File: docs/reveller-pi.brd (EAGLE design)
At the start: 23 parts, among them Q1 BS270, Q2 BS270, T1 2N2222, X1 CANTON-POWER, X2 RASPI_BOARD_AB_E0, X3 PG203J

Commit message: Cleaned
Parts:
- moved Q2 2.22 mm to (54.0, 38.6)
- moved R5 0.57 mm to (54.0, 28.2)
- moved R2 0.13 mm to (27.6, 45.4)
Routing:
- net +5V: track 27.6 -> 26.0 mm
- net PWCTL: track 71.3 -> 70.6 mm
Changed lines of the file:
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@@
 <text x="76.327" y="35.56" size="1.27" layer="29" font="vector">R1</text>
 <text x="76.327" y="35.56" size="1.27" layer="31" font="vector">R1</text>
-<text x="54.102" y="26.924" size="1.27" layer="31" font="vector" rot="R90">R5</text>
-<text x="54.102" y="26.924" size="1.27" layer="29" font="vector" rot="R90">R5</text>
+<text x="54.483" y="27.178" size="1.27" layer="31" font="vector" rot="R90">R5</text>
+<text x="54.483" y="27.178" size="1.27" layer="29" font="vector" rot="R90">R5</text>
 <text x="54.102" y="51.308" size="1.27" layer="29" font="vector">R4</text>
 <text x="54.102" y="51.308" size="1.27" layer="31" font="vector">R4</text>
@@
 <element name="Q1" library="transistor-fet" package="TO92-" value="BS270" x="53.9115" y="46.863" rot="R270"/>
 <element name="R1" library="rcl" package="0204/7" value="1k" x="77.343" y="36.195"/>
-<element name="R2" library="rcl" package="0204/7" value="3.3k" x="27.47988125" y="45.370990625" rot="R140"/>
+<element name="R2" library="rcl" package="0204/7" value="3.3k" x="27.60688125" y="45.370990625" rot="R140"/>
 <element name="R3" library="rcl" package="0204/7" value="10k" x="45.7835" y="43.053" rot="R90"/>
 <element name="R4" library="rcl" package="0204/7" value="10k" x="55.118" y="51.943" rot="R180"/>
@@
 <element name="C2" library="rcl" package="E2,5-5" value="470pF" x="34.29" y="43.688" rot="R180"/>
 <element name="C1" library="rcl" package="E2,5-5" value="470pF" x="40.0685" y="43.7515" rot="R180"/>
-<element name="Q2" library="transistor-fet" package="TO92-" value="BS270" x="53.467" y="36.449" rot="R270"/>
-<element name="R5" library="rcl" package="0204/7" value="100k" x="53.467" y="27.94" rot="R270"/>
+<element name="Q2" library="transistor-fet" package="TO92-" value="BS270" x="53.975" y="38.608" rot="R270"/>
+<element name="R5" library="rcl" package="0204/7" value="100k" x="53.975" y="28.194" rot="R270"/>
 <element name="T1" library="transistor" package="TO18" value="2N2222" x="65.405" y="22.606" rot="R270"/>
 <element name="R6" library="rcl" package="0204/7" value="10K" x="77.343" y="32.385"/>
@@
 <contactref element="C8" pad="+"/>
 <contactref element="Q2" pad="3"/>
-<wire x1="51.181" y1="53.594" x2="57.277" y2="53.594" width="0.8128" layer="1"/>
+<wire x1="50.038" y1="53.594" x2="57.277" y2="53.594" width="0.8128" layer="1"/>
 <wire x1="57.277" y1="53.594" x2="58.928" y2="51.943" width="0.8128" layer="1"/>
-<wire x1="51.181" y1="53.594" x2="50.038" y2="53.594" width="0.8128" layer="1"/>
-<wire x1="50.038" y1="53.594" x2="50.038" y2="38.989" width="0.8128" layer="1"/>
-<wire x1="50.038" y1="38.989" x2="53.467" y2="38.989" width="0.8128" layer="1"/>
+<wire x1="50.038" y1="53.594" x2="50.038" y2="41.148" width="0.8128" layer="1"/>
+<wire x1="50.038" y1="41.148" x2="53.975" y2="41.148" width="0.8128" layer="1"/>
 </signal>
 <signal name="RESET">
 <contactref element="R2" pad="1"/>
 <contactref element="SID" pad="5"/>
-<wire x1="30.48" y1="35.56" x2="30.398509375" y2="42.92196875" width="1.016" layer="1"/>
+<wire x1="30.48" y1="35.56" x2="30.525509375" y2="42.92196875" width="1.016" layer="1"/>
 </signal>
 <signal name="+3V3">
@@
 <contactref element="R5" pad="1"/>
 <contactref element="Q2" pad="1"/>
-<wire x1="53.467" y1="31.75" x2="53.467" y2="33.909" width="0.8128" layer="16"/>
-<wire x1="53.467" y1="33.909" x2="57.531" y2="33.909" width="0.8128" layer="16"/>
-<wire x1="57.531" y1="33.909" x2="57.531" y2="46.863" width="0.8128" layer="16"/>
+<wire x1="53.975" y1="32.004" x2="53.975" y2="36.068" width="0.8128" layer="16"/>
+<wire x1="53.975" y1="36.068" x2="57.531" y2="36.068" width="0.8128" layer="16"/>
+<wire x1="57.531" y1="36.068" x2="57.531" y2="46.863" width="0.8128" layer="16"/>
 <wire x1="57.531" y1="46.863" x2="53.9115" y2="46.863" width="0.8128" layer="16"/>
 </signal>
@@
 <contactref element="Q2" pad="2"/>
 <contactref element="SID" pad="25"/>
-<wire x1="53.467" y1="36.449" x2="47.498" y2="36.449" width="0.8128" layer="16"/>
-<wire x1="47.498" y1="36.449" x2="33.02" y2="21.971" width="0.8128" layer="16"/>
+<wire x1="53.975" y1="38.608" x2="48.514" y2="34.417" width="0.8128" layer="16"/>
+<wire x1="48.514" y1="34.417" x2="33.02" y2="21.971" width="0.8128" layer="16"/>
 <wire x1="33.02" y1="21.971" x2="33.02" y2="20.32" width="0.8128" layer="16"/>
 </signal>

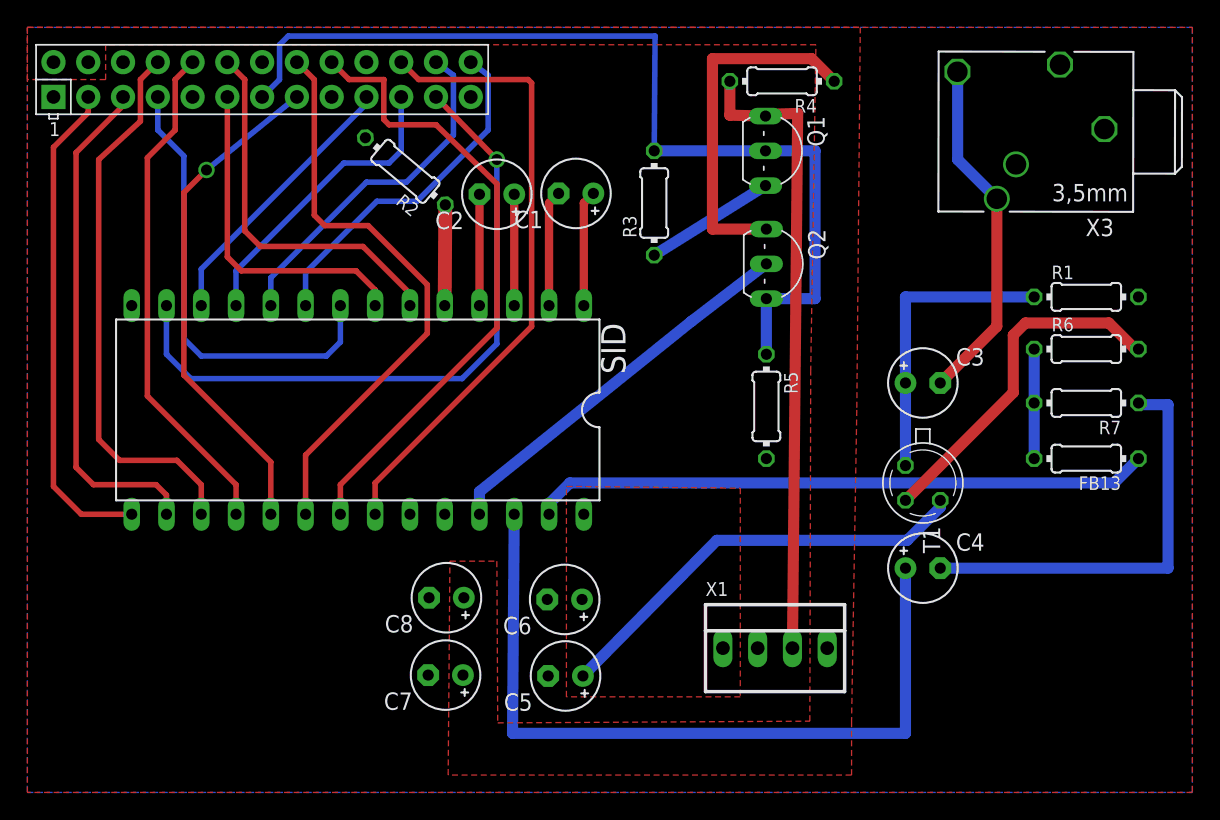
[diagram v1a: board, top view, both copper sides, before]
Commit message: Revised boarddesign and schmatic for better powercontrol
Cleaned up the board with, everything done by Morten Leikvoll.
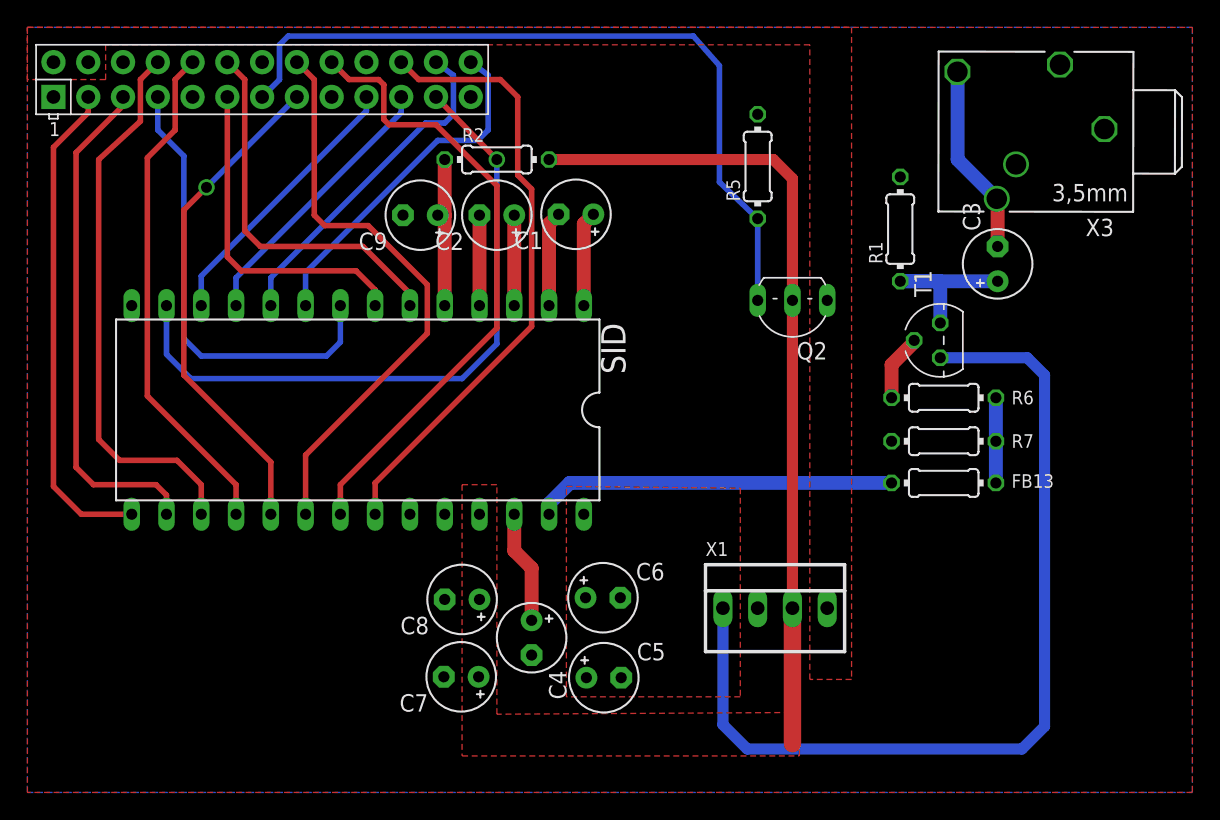
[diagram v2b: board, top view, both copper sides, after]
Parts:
- removed Q1: BS270, transistor-fet:TO92-
- removed R3, R4: 10k, rcl:0204/7
- added C9: 0.1uF, rcl:E2,5-5
- T1: value 2N2222 -> BC547; device transistor:TO18 -> transistor:TO92
- moved C4 29.0 mm to (36.8, 11.3), turned to 270 degrees
- moved R5 17.5 mm to (53.3, 45.7), turned to 90 degrees
- moved R1 14.5 mm to (63.8, 41.1), turned to 90 degrees
- moved R6 11.0 mm to (66.9, 28.8), turned to 180 degrees
- moved R7 10.8 mm to (66.9, 25.7), turned to 0 degrees
- moved FB13 10.6 mm to (66.9, 22.6), turned to 0 degrees
- moved T1 10.5 mm to (66.7, 33.0), turned to 90 degrees
- moved C3 10.3 mm to (70.9, 38.6), turned to 90 degrees
- moved R2 6.74 mm to (34.3, 46.2), turned to 0 degrees
- moved Q2 3.28 mm to (55.9, 35.9), turned to 180 degrees
- moved X1 2.92 mm to (54.6, 13.5)
- moved C5 2.80 mm to (42.1, 8.38), turned to 0 degrees
- moved C6 2.80 mm to (42.0, 14.2), turned to 0 degrees
- moved C1 1.52 mm to (40.1, 42.2)
- moved C2 1.52 mm to (34.3, 42.2)
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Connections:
- net N$1 renamed CAPX
- net N$2 renamed AUDIO_DC
- net N$3 renamed AUDIO_OUT
- net N$5 renamed AUDIO_PREAMP_B
- net N$6 renamed AUDIO_RAW
- net N$8 renamed AUDIO_PREAMP
- removed net N$4: Q1.3, R4.2, X1.3
- removed net N$7: R5.2
- net +3V3: no longer Q1.1, R2.2, R3.1
- net +5V: no longer C7.+, C8.+, R4.1
- net +5V_SID: now also C7.+, C8.+, R2.2, X1.3
- net GND: now also C9.-, R5.2
- net PWCTL: no longer Q1.2, R3.2
- net RESET: now also C9.+
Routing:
- net CAPX: track 56.8 -> 8.27 mm
- net N$4: track 46.5 -> 0.00 mm
- net +12V: track 31.7 -> 67.2 mm
- net +5V_SID: track 28.4 -> 59.6 mm
- net GND: track 30.9 -> 0.00 mm
- net +5V: track 26.0 -> 0.00 mm
- net AUDIO_PREAMP_B: track 25.6 -> 4.87 mm
- net AUDIO_RAW: track 45.3 -> 26.4 mm
- net PWCTL: track 70.6 -> 56.0 mm
- net AUDIO_OUT: track 26.2 -> 14.6 mm
- net +3V3: track 9.58 -> 0.00 mm
- net AUDIO_DC: track 21.7 -> 13.1 mm
- net RESET: track 7.36 -> 11.2 mm
- net A2: track 22.2 -> 20.2 mm
- net AUDIO_PREAMP: track 8.00 -> 6.22 mm
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- added copper zone on layer 1, net +5V_SID
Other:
- board text removed: "C3"
- board text removed: "C4"
- board text removed: "C5"
- board text removed: "C6"
- board text removed: "C7"
- board text removed: "C8"
- board text removed: "FB13"
- board text removed: "R1"
- board text removed: "R2"
- board text removed: "R3"
- board text removed: "R4"
- board text removed: "R5"
- board text removed: "R6"
- board text removed: "R7"
- board text removed: "T1"

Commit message: More revisions...
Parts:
- FB13: value (none) -> 0R
- SID: value (none) -> 6581
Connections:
- removed net +3V3: X2.1, X2.17
- new net 3V3: X2.1
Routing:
- net +12V: track 67.2 -> 32.3 mm
- net +5V_SID: track 59.6 -> 27.2 mm
- net A0: track 25.6 -> 22.8 mm
- net A1: track 24.8 -> 22.8 mm
- net D5: track 42.5 -> 40.6 mm
- net PWCTL: track 56.0 -> 55.1 mm
- added copper zone on layer 1, net GND
- removed copper zone on layer 1, net +3V3
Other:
- board outline added: 85.1 x 55.9 mm
- board text added: "5V_SID"
- board text removed: "3.3V"

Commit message: Completed powercontrol and boarddesign
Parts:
- removed Q2: BS270, transistor-fet:TO92-
- removed R5: 100k, rcl:0204/7
- added Q100: IRF9Z24N, transistor-power:TO220BV
- added R105: NM*, rcl:0204/7
- renumbered C1 to C104, C2 to C103, C3 to C102, C4 to C101, C5 to C105, C6 to C106, C7 to C107, C8 to C108, C9 to C100, FB13 to R103, R1 to R101, R2 to R102, R6 to R104, R7 to R100, SID to IC100, T1 to T100, X1 to X102, X2 to X100, X3 to X101
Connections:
- net +5V: now also Q100.S, R105.2; no longer Q2.3
- net +5V_SID: now also Q100.D; no longer Q2.2, X102.3
- net GND: no longer R5.2
- net PWCTL: now also Q100.G, R105.1, X102.3; no longer Q2.1, R5.1
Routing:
- net +5V_SID: track 27.2 -> 0.00 mm
- net PWCTL: track 55.1 -> 78.7 mm
- net CS: track 33.5 -> 20.8 mm
- net D7: track 45.2 -> 39.6 mm
- net RW: track 24.6 -> 19.7 mm
- net CLK: track 27.7 -> 23.3 mm
- net D6: track 46.0 -> 41.8 mm
- net A4: track 49.3 -> 45.6 mm
- net D4: track 36.5 -> 38.6 mm, vias 1 -> 0
- net D3: track 37.1 -> 39.0 mm

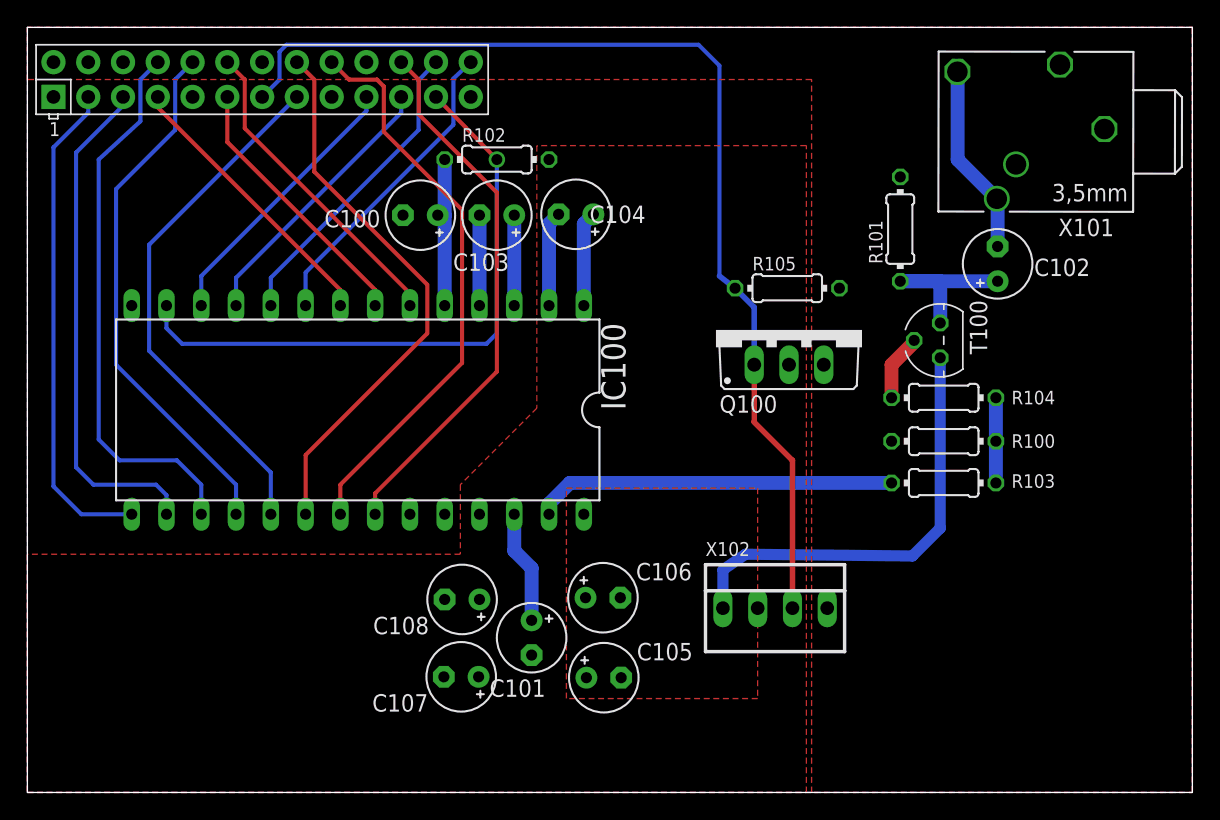
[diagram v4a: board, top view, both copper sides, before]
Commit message: Changed from holemounted caps and res to SMDs
Changed to get a better board design, Morten Leikvoll did all of this
because he ment he would look more nice with some of the caps and res.
on the backside og the board.
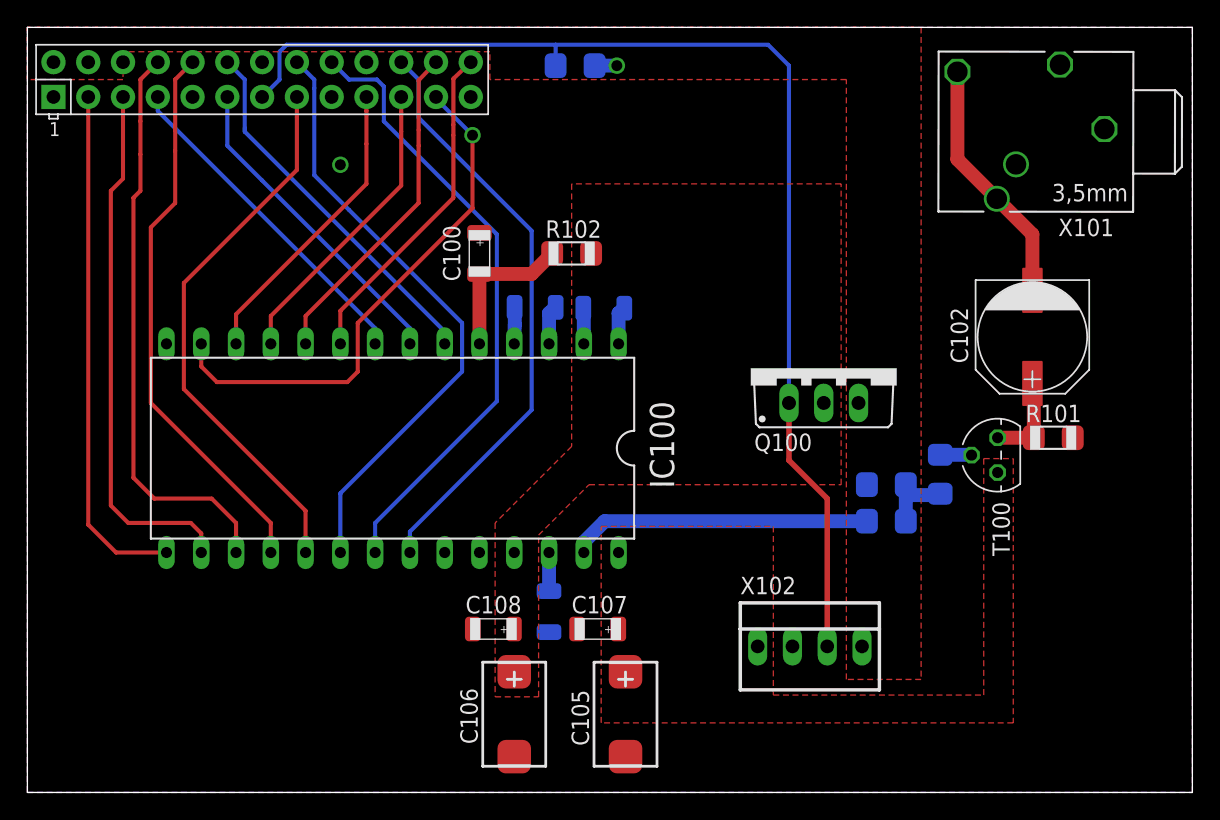
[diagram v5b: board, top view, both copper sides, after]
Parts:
- C100, C107: value 0.1uF -> 100nF; device rcl:E2,5-5 -> cyviz:SMD-IPC_C1206
- C101, C103, C104: device rcl:E2,5-5 -> cyviz:SMD-IPC_C1206
- C102: device rcl:E2,5-5 -> cyviz:PXE-H
- C105: value 0.1uF -> 10uF; device rcl:E2,5-5 -> cyviz:SMD-IPC_CT7343
- C106: device rcl:E2,5-5 -> cyviz:SMD-IPC_CT7343
- C108: value 10uF -> 100nF; device rcl:E2,5-5 -> cyviz:SMD-IPC_C1206
- R100, R101, R102, R103, R104, R105: device rcl:0204/7 -> cyviz:SMD-IPC_R1206
- moved R105 22.5 mm to (40.0, 53.1), flipped to the bottom, turned to 180 degrees
- moved R101 18.9 mm to (74.9, 25.9), turned to 0 degrees
- moved C106 10.7 mm to (35.6, 5.71), turned to 270 degrees
- moved C107 10.6 mm to (41.7, 11.9), turned to 0 degrees
- moved T100 9.37 mm to (70.9, 24.6)
- moved R102 8.77 mm to (39.8, 39.4)
- moved C103 7.29 mm to (37.1, 35.4), flipped to the bottom, turned to 0 degrees
- moved C104 7.15 mm to (42.1, 35.4), flipped to the bottom, turned to 0 degrees
- moved C102 5.91 mm to (73.4, 33.3), turned to 270 degrees
- moved R104 5.59 mm to (66.7, 23.2), flipped to the bottom, turned to 90 degrees
- moved R100 5.26 mm to (62.7, 22.5), flipped to the bottom, turned to 180 degrees
- moved C100 5.14 mm to (33.0, 39.4), turned to 90 degrees
- moved R103 5.04 mm to (62.7, 19.8), flipped to the bottom, turned to 180 degrees
- moved IC100 3.78 mm to (26.7, 25.1)
- moved X102 3.78 mm to (57.1, 10.7)
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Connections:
- net +12V: now also C107.+; no longer C106.+
- net +5V_SID: now also C106.+; no longer C107.+
- net CAP1A: now also C104.-; no longer C104.+
- net CAP1B: now also C104.+; no longer C104.-
- net CAP2A: now also C103.-; no longer C103.+
- net CAP2B: now also C103.+; no longer C103.-
- net GND: now also C100.+; no longer C100.-
- net RESET: now also C100.-; no longer C100.+
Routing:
- net +12V: track 32.3 -> 0.00 mm
- net PWCTL: track 78.7 -> 87.0 mm
- net A4: track 45.6 -> 38.5 mm
- net AUDIO_DC: track 13.1 -> 6.71 mm
- net CAPX: track 8.27 -> 2.82 mm
- net CS: track 20.8 -> 25.4 mm
- net CAP1B: track 6.96 -> 2.61 mm
- net AUDIO_RAW: track 26.4 -> 22.1 mm
- net CAP1A: track 6.96 -> 2.80 mm
- net CAP2B: track 6.60 -> 2.67 mm
- net RW: track 19.7 -> 23.6 mm
- net D6: track 41.8 -> 45.7 mm
- net CLK: track 23.3 -> 27.1 mm
- net D5: track 40.6 -> 44.5 mm
- net D7: track 39.6 -> 43.4 mm
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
